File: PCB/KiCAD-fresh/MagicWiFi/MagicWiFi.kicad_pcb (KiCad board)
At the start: 2 copper layers, 6 parts

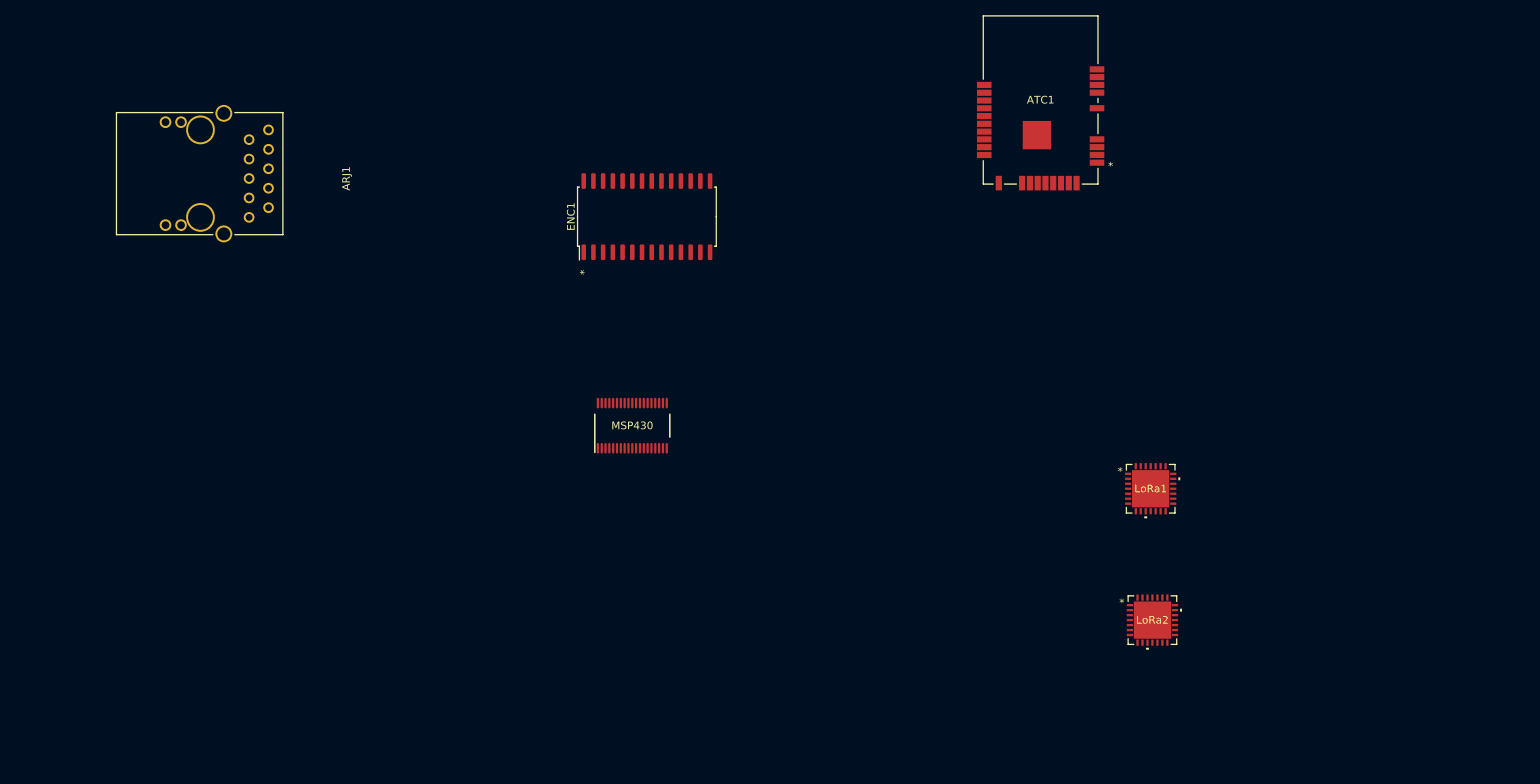
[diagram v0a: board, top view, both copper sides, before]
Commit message: Added basic layout
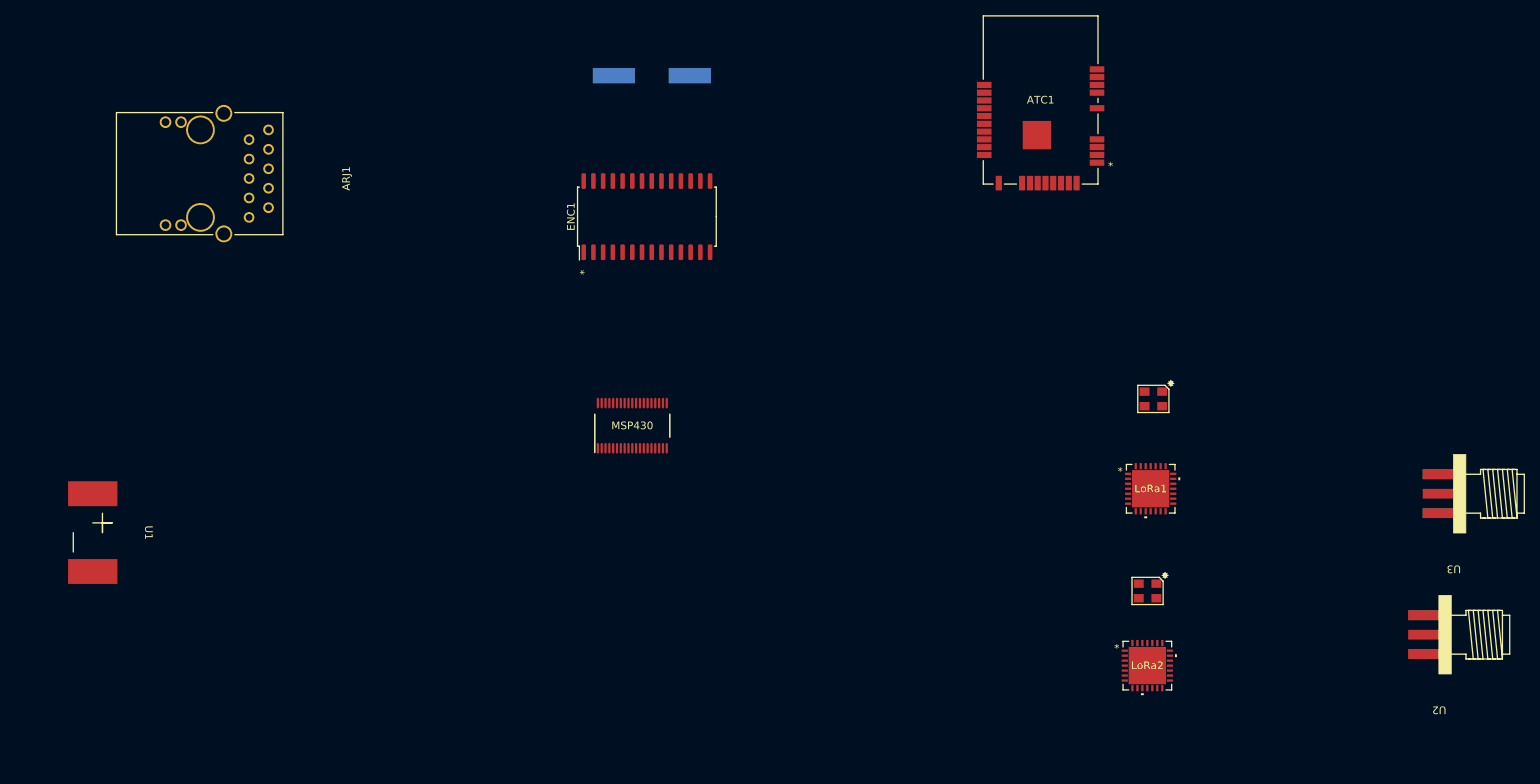
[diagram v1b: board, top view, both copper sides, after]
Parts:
- added U1: ~, MagicWiFi:Barrel_Conn, F.Cu at (38.1, 99.1)
- added U2: ~, MagicWiFi:SMA_EDGELAUNCH, F.Cu at (217.2, 112.4)
- added U3: ~, MagicWiFi:SMA_EDGELAUNCH, F.Cu at (219.1, 94.0)
- added X1: Osc, MagicWiFi:TCXO, F.Cu at (179.1, 106.7)
- added X2: Osc, MagicWiFi:TCXO, F.Cu at (179.8, 81.6)
- added X3: Osc, MagicWiFi:Xosc, B.Cu at (114.3, 39.4)
- moved LoRa2 5.98 mm to (179.0, 116.4)
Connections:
- ARJ1 pad 15: unconnected-(ARJ1-GND-Pad15) -> /GND
- ARJ1 pad 16: unconnected-(ARJ1-GND-Pad16) -> /GND
- ARJ1 pad 2: unconnected-(ARJ1-VC1--Pad2) -> /GND
- ARJ1 pad 7: unconnected-(ARJ1-VC1+-Pad7) -> /GND
- ATC1 pad 12: unconnected-(ATC1-GND_2-Pad12) -> /GND
- ATC1 pad 20: unconnected-(ATC1-VBAT-Pad20) -> /3v3
- ATC1 pad 23: unconnected-(ATC1-VDDIO-Pad23) -> /3v3
- ATC1 pad 28: unconnected-(ATC1-GND_3-Pad28) -> /GND
- ATC1 pad 29: unconnected-(ATC1-GND_PADDLE-Pad29) -> /GND
- ATC1 pad 9: unconnected-(ATC1-GND_1-Pad9) -> /GND
- ENC1 pad 11: unconnected-(ENC1-VSSRX-Pad11) -> /GND
- ENC1 pad 15: unconnected-(ENC1-VDDTX-Pad15) -> /3v3
- ENC1 pad 18: unconnected-(ENC1-VSSTX-Pad18) -> /GND
- ENC1 pad 19: unconnected-(ENC1-VDDRX-Pad19) -> /3v3
- ENC1 pad 2: unconnected-(ENC1-VSS-Pad2) -> /GND
- ENC1 pad 20: unconnected-(ENC1-VDDPLL-Pad20) -> /3v3
- ENC1 pad 21: unconnected-(ENC1-VSSPLL-Pad21) -> /GND
- ENC1 pad 22: unconnected-(ENC1-VSSOSC-Pad22) -> /GND
- ENC1 pad 25: unconnected-(ENC1-VDDOSC-Pad25) -> /3v3
- ENC1 pad 28: unconnected-(ENC1-VDD-Pad28) -> /3v3
- LoRa1 pad 1: unconnected-(LoRa1-VBAT1-Pad1) -> /3v3
- LoRa1 pad 15: unconnected-(LoRa1-VBAT2-Pad15) -> /3v3
- LoRa1 pad 16: unconnected-(LoRa1-GND-Pad16) -> /GND
- LoRa1 pad 22: unconnected-(LoRa1-GND-Pad22) -> /GND
- LoRa1 pad 26: unconnected-(LoRa1-GND-Pad26) -> /GND
- LoRa1 pad 29: unconnected-(LoRa1-GND-Pad29) -> /GND
- LoRa2 pad 1: unconnected-(LoRa2-VBAT1-Pad1) -> /3v3
- LoRa2 pad 15: unconnected-(LoRa2-VBAT2-Pad15) -> /3v3
- LoRa2 pad 16: unconnected-(LoRa2-GND-Pad16) -> /GND
- LoRa2 pad 22: unconnected-(LoRa2-GND-Pad22) -> /GND
- LoRa2 pad 26: unconnected-(LoRa2-GND-Pad26) -> /GND
- LoRa2 pad 29: unconnected-(LoRa2-GND-Pad29) -> /GND
- MSP430 pad 10: unconnected-(MSP430-DVCC-Pad10) -> /3v3
- MSP430 pad 11: unconnected-(MSP430-DVSS-Pad11) -> /GND

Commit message: part way through PCB design
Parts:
- added C1: 10uF, Resistor_SMD:R_0805_2012Metric_Pad1.20x1.40mm_HandSolder, F.Cu at (104.8, 66.7)
- added J1: 702461402, MagicWiFi:CON_702461402_MOL, F.Cu at (123.2, 120.0)
- added R1: 60, Resistor_SMD:R_0805_2012Metric_Pad1.20x1.40mm_HandSolder, F.Cu at (52.7, 39.4)
- added R2: 60, Resistor_SMD:R_0805_2012Metric_Pad1.20x1.40mm_HandSolder, F.Cu at (52.7, 65.4)
- added R3: 2.32k 1%, Resistor_SMD:R_0805_2012Metric_Pad1.20x1.40mm_HandSolder, F.Cu at (122.6, 67.3)
- added R4: 47k, Resistor_SMD:R_0805_2012Metric_Pad1.20x1.40mm_HandSolder, F.Cu at (43.8, 108.6)
- added SW1: SW_Push_Open, MagicWiFi:KSR223GNCLFG, F.Cu at (35.6, 114.3)
- moved BATT1 25.1 mm to (31.2, 123.2)
- renumbered U2 to AN1, U3 to AN2, U1 to BATT1
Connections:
- ARJ1 pad 11: unconnected-(ARJ1-LEDG+-Pad11) -> Net-(ARJ1-LEDG+)
- ARJ1 pad 12: unconnected-(ARJ1-LEDG--Pad12) -> /~LEDG
- ARJ1 pad 13: unconnected-(ARJ1-LEDY+-Pad13) -> Net-(ARJ1-LEDY+)
- ARJ1 pad 14: unconnected-(ARJ1-LEDY--Pad14) -> /~LEDY
- ENC1 pad 1: unconnected-(ENC1-VCAP-Pad1) -> Net-(ENC1-VCAP)
- ENC1 pad 14: unconnected-(ENC1-RBIAS-Pad14) -> Net-(ENC1-RBIAS)
- ENC1 pad 26: unconnected-(ENC1-LEDB-Pad26) -> /~LEDY
- ENC1 pad 27: unconnected-(ENC1-LEDA-Pad27) -> /~LEDG
- MSP430 pad 9: unconnected-(MSP430-RST_NMI_SBWTDIO_N-Pad9) -> Net-(MSP430-RST_NMI_SBWTDIO_N)

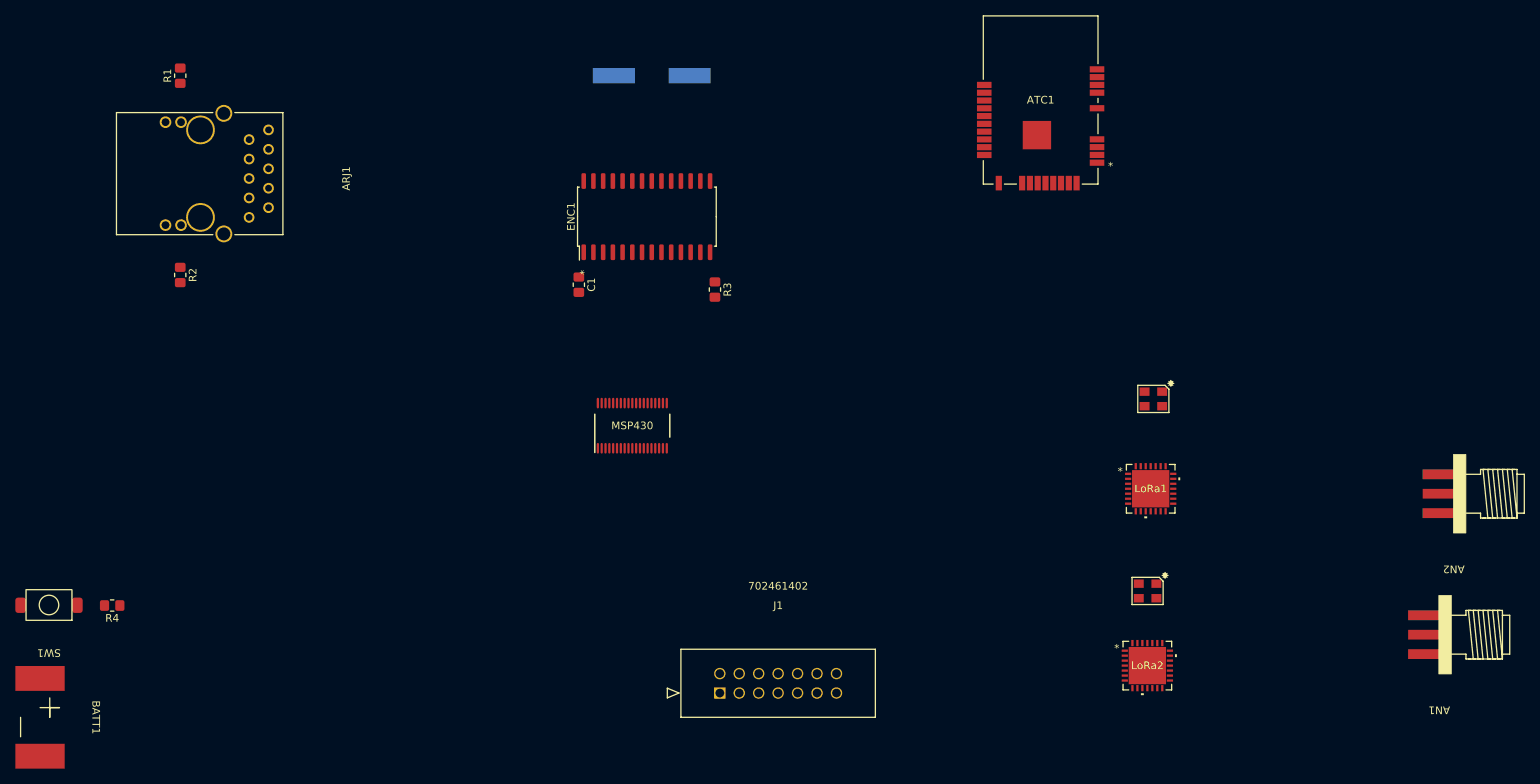
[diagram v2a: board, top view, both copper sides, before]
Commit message: Antenna Design Remade, stolen shamelessly from Sample design by SemTech (Mfgr), other traces routed and Documentation refreshed for components
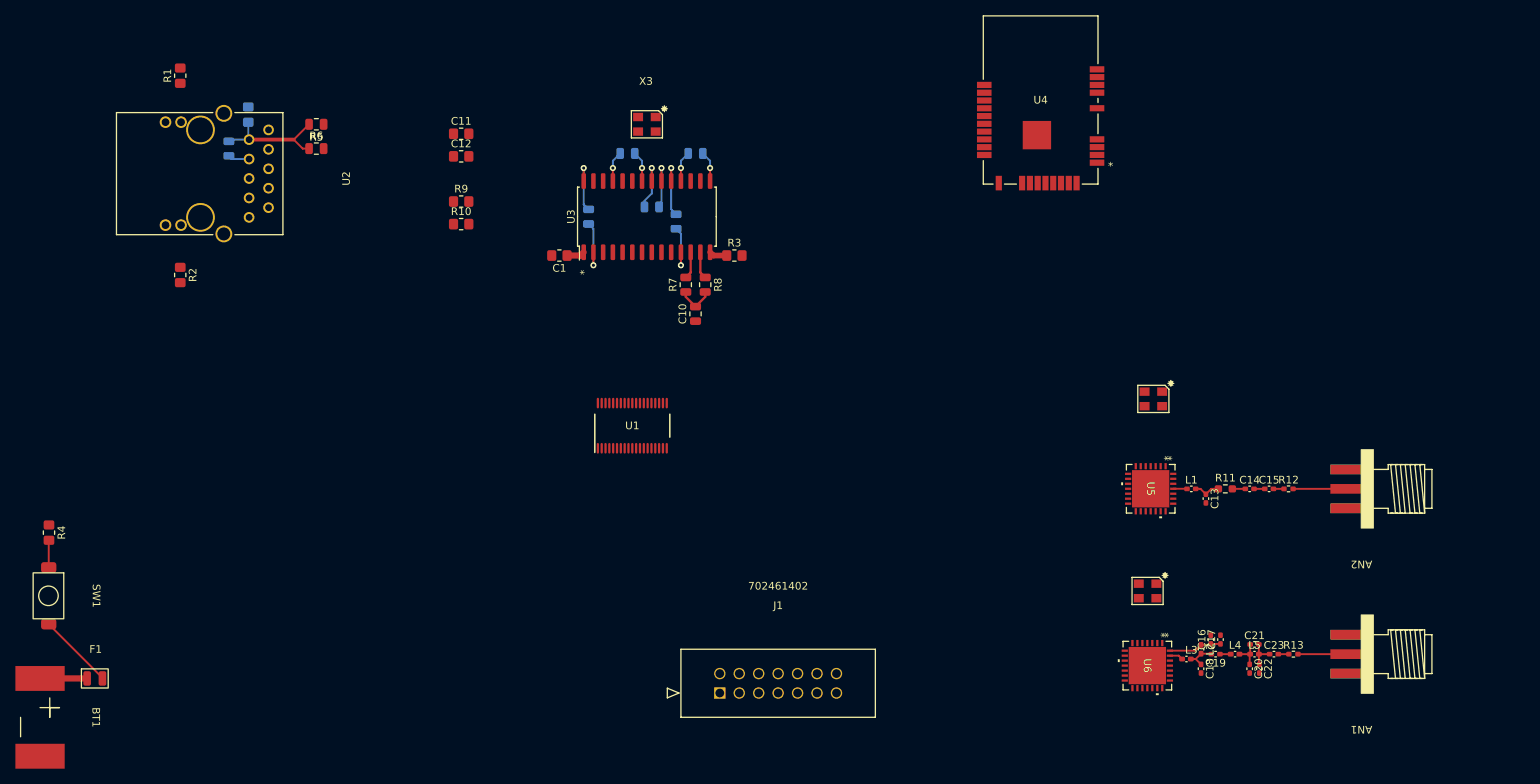
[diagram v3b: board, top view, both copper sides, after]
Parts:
- added C10: 0.1 uF, Capacitor_SMD:C_0805_2012Metric, F.Cu at (120.0, 70.5)
- added C11: 0.1 nF, Resistor_SMD:R_0805_2012Metric_Pad1.20x1.40mm_HandSolder, F.Cu at (89.4, 47.0)
- added C12: 0.1 nF, Resistor_SMD:R_0805_2012Metric_Pad1.20x1.40mm_HandSolder, F.Cu at (89.4, 49.9)
- added C13: 3.3 pF, Capacitor_SMD:C_0402_1005Metric_Pad0.74x0.62mm_HandSolder, F.Cu at (186.7, 94.6)
- added C14: 47 pF, Capacitor_SMD:C_0402_1005Metric_Pad0.74x0.62mm_HandSolder, F.Cu at (192.4, 93.3)
- added C15: 47 pF, Capacitor_SMD:C_0402_1005Metric_Pad0.74x0.62mm_HandSolder, F.Cu at (194.9, 93.3)
- added C16: 10 nF, Capacitor_SMD:C_0402_1005Metric_Pad0.74x0.62mm_HandSolder, F.Cu at (187.3, 113.0)
- added C17: 47 pF, Capacitor_SMD:C_0402_1005Metric_Pad0.74x0.62mm_HandSolder, F.Cu at (188.6, 113.0)
- added C18: 8.2 pF, Capacitor_SMD:C_0402_1005Metric_Pad0.74x0.62mm_HandSolder, F.Cu at (186.1, 116.8)
- added C19: 22 pF, Capacitor_SMD:C_0402_1005Metric_Pad0.74x0.62mm_HandSolder, F.Cu at (188.0, 114.9)
- added C20: 8.2 pF, Capacitor_SMD:C_0402_1005Metric_Pad0.74x0.62mm_HandSolder, F.Cu at (192.4, 116.8)
- added C21: 1.5 pF, Capacitor_SMD:C_0402_1005Metric_Pad0.74x0.62mm_HandSolder, F.Cu at (193.0, 113.7)
- added C22: 3.3 pF, Capacitor_SMD:C_0402_1005Metric_Pad0.74x0.62mm_HandSolder, F.Cu at (193.7, 116.8)
- added C23: 47 pF, Capacitor_SMD:C_0402_1005Metric_Pad0.74x0.62mm_HandSolder, F.Cu at (195.6, 114.9)
- added C4: 0.1 uF, Capacitor_SMD:C_0805_2012Metric, B.Cu at (59.1, 48.9)
- added C5: 0.1 uF, Capacitor_SMD:C_0805_2012Metric, B.Cu at (117.5, 58.4)
- added C6: 0.1 uF, Capacitor_SMD:C_0805_2012Metric, B.Cu at (120.0, 49.5)
- added C7: 0.1 uF, Capacitor_SMD:C_0805_2012Metric, B.Cu at (111.1, 49.5)
- added C8: 0.1 uF, Capacitor_SMD:C_0805_2012Metric, B.Cu at (114.3, 56.5)
- added C9: 0.1 uF, Capacitor_SMD:C_0805_2012Metric, B.Cu at (106.0, 57.8)
- added F1: Polyfuse, MagicWiFi:Fuse_BelFuse_0ZCJ0_1206_Metric_3216, F.Cu at (41.5, 118.1)
- added FB1: 80 mA min, Resistor_SMD:R_0805_2012Metric_Pad1.20x1.40mm_HandSolder, B.Cu at (61.6, 44.5)
- added L1: 10 nH, Capacitor_SMD:C_0402_1005Metric_Pad0.74x0.62mm_HandSolder, F.Cu at (184.8, 93.3)
- added L2: 33 nH, Inductor_SMD:L_0402_1005Metric_Pad0.77x0.64mm_HandSolder, F.Cu at (186.1, 114.3)
- added L3: 2.7 nH, Inductor_SMD:L_0402_1005Metric_Pad0.77x0.64mm_HandSolder, F.Cu at (184.2, 115.6)
- added L4: 5.6 nH, Inductor_SMD:L_0402_1005Metric_Pad0.77x0.64mm_HandSolder, F.Cu at (190.5, 114.9)
- added L5: 5.6 nH, Inductor_SMD:L_0402_1005Metric_Pad0.77x0.64mm_HandSolder, F.Cu at (193.0, 114.9)
- added R10: 75 Ohm, Resistor_SMD:R_0805_2012Metric_Pad1.20x1.40mm_HandSolder, F.Cu at (89.4, 58.8)
- added R11: 0R, Resistor_SMD:R_0603_1608Metric_Pad0.98x0.95mm_HandSolder, F.Cu at (189.2, 93.3)
- added R12: 0R, Resistor_SMD:R_0402_1005Metric_Pad0.72x0.64mm_HandSolder, F.Cu at (197.5, 93.3)
- added R13: 0R, Resistor_SMD:R_0402_1005Metric_Pad0.72x0.64mm_HandSolder, F.Cu at (198.1, 114.9)
- added R5: 49.9 Ohm, Capacitor_SMD:C_0805_2012Metric, F.Cu at (70.5, 45.7)
- added R6: 49.9 Ohm, Capacitor_SMD:C_0805_2012Metric, F.Cu at (70.5, 48.9)
- added R7: 49.9 Ohm, Capacitor_SMD:C_0805_2012Metric, F.Cu at (118.7, 66.7)
- added R8: 49.9 Ohm, Capacitor_SMD:C_0805_2012Metric, F.Cu at (121.3, 66.7)
- added R9: 75 Ohm, Resistor_SMD:R_0805_2012Metric_Pad1.20x1.40mm_HandSolder, F.Cu at (89.4, 55.8)
- SW1: value SW_Push_Open -> SPST-NC
- U1: renamed from MSP430; value MSP430FR2355TDBTR -> MSP430
- U2: renamed from ARJ1; value ARJM11C7-114-BA-EW2 -> ARJ1
- U3: renamed from ENC1; value ENC28J60x-SO -> ENC
- U4: renamed from ATC1; value ATWINC1500-MR210PB1952-T -> ATC
- U5: renamed from LoRa1; value SX1272IMLTRT -> LoRa1
- U6: renamed from LoRa2; value SX1272IMLTRT -> LoRa2
- X3: footprint MagicWiFi:Xosc -> MagicWiFi:TCXO; moved to F.Cu
- moved R4 12.6 mm to (35.6, 99.1), turned to -90 degrees
- moved AN2 12.1 mm to (207.0, 93.3)
- moved AN1 10.5 mm to (207.0, 114.9)
- moved SW1 8.98 mm to (41.2, 107.3), turned to -90 degrees
- moved X3 6.38 mm to (113.7, 45.7), turned to 0 degrees
- moved R3 5.12 mm to (125.1, 62.9), turned to 0 degrees
- moved C1 4.58 mm to (102.2, 62.9), turned to 180 degrees
- turned U5 to -90 degrees
- turned U6 to -90 degrees
- renumbered BATT1 to BT1
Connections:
- net /~LEDG renamed /LEDGN
- net /~LEDY renamed /LEDYN
- AN1 pad 1: unconnected-(AN1-In-Pad1) -> Net-(AN1-In)
- AN1 pad 2: unconnected-(AN1-GND-Pad2) -> GND
- AN1 pad 3: unconnected-(AN1-GND-Pad3) -> GND
- AN1 pad 4: unconnected-(AN1-GND-Pad4) -> GND
- AN1 pad 5: unconnected-(AN1-GND-Pad5) -> GND
- AN2 pad 1: unconnected-(AN2-In-Pad1) -> Net-(AN2-In)
- AN2 pad 2: unconnected-(AN2-GND-Pad2) -> GND
- AN2 pad 3: unconnected-(AN2-GND-Pad3) -> GND
- AN2 pad 4: unconnected-(AN2-GND-Pad4) -> GND
- AN2 pad 5: unconnected-(AN2-GND-Pad5) -> GND
- BT1 pad 1: /3v3 -> Net-(BT1-Inner1)
- BT1 pad 2: /GND -> GND
- C1 pad 2: /GND -> GND
- J1 pad 1: unconnected-(J1-Pad1) -> /ETH_MOSI
- J1 pad 10: unconnected-(J1-Pad10) -> /~MSP_RST
- J1 pad 2: unconnected-(J1-Pad2) -> /MSP_VCC
- J1 pad 3: unconnected-(J1-Pad3) -> /ETH_MISO
- J1 pad 4: unconnected-(J1-Pad4) -> /MSP_VCC_TAR
- J1 pad 5: unconnected-(J1-Pad5) -> /ETH_CLK
- J1 pad 7: unconnected-(J1-Pad7) -> /~ETH_CHIPSEL
- J1 pad 8: unconnected-(J1-Pad8) -> /MSP_TEST
- J1 pad 9: unconnected-(J1-Pad9) -> GND
- R1 pad 2: /3v3 -> +3.3V
- R2 pad 2: /3v3 -> +3.3V
- R3 pad 2: /GND -> GND
- SW1 pad 2: /3v3 -> +3.3V
- U1 pad 10: /3v3 -> +3.3V
- U1 pad 11: /GND -> GND
- U2 pad 1: unconnected-(ARJ1-VC2--Pad1) -> /VC2ETH_N
- U2 pad 10: unconnected-(ARJ1-TD+-Pad10) -> /TD_P
- U2 pad 15: /GND -> GND
- U2 pad 16: /GND -> GND
- U2 pad 2: /GND -> GND
- U2 pad 3: unconnected-(ARJ1-RD--Pad3) -> /RD_N
- U2 pad 5: unconnected-(ARJ1-RD+-Pad5) -> /RD_P
- U2 pad 6: unconnected-(ARJ1-VC2+-Pad6) -> /VC2ETH_P
- U2 pad 7: /GND -> GND
- U2 pad 8: unconnected-(ARJ1-TD--Pad8) -> /TD_N
- U2 pad 9: unconnected-(ARJ1-TCT-Pad9) -> /TD_C
- U3 pad 10: unconnected-(ENC1-~{RESET}-Pad10) -> /~ETH_RST
- U3 pad 11: /GND -> GND
- U3 pad 12: unconnected-(ENC1-TPIN--Pad12) -> /RD_N
- U3 pad 13: unconnected-(ENC1-TPIN+-Pad13) -> /RD_P
- U3 pad 15: /3v3 -> +3.3V
- U3 pad 16: unconnected-(ENC1-TPOUT--Pad16) -> /TD_N
- U3 pad 17: unconnected-(ENC1-TPOUT+-Pad17) -> /TD_P
- U3 pad 18: /GND -> GND
- U3 pad 19: /3v3 -> +3.3V
- U3 pad 2: /GND -> GND
- U3 pad 20: /3v3 -> +3.3V
- U3 pad 21: /GND -> GND
- U3 pad 22: /GND -> GND
- U3 pad 23: unconnected-(ENC1-OSC1-Pad23) -> /OSC1_ETH
- U3 pad 25: /3v3 -> +3.3V
- U3 pad 28: /3v3 -> +3.3V
- U3 pad 4: unconnected-(ENC1-~{INT}-Pad4) -> /~ETH_IRQ
- U3 pad 6: unconnected-(ENC1-SO-Pad6) -> /ETH_MISO
- U3 pad 7: unconnected-(ENC1-SI-Pad7) -> /ETH_MOSI
- U3 pad 8: unconnected-(ENC1-SCK-Pad8) -> /ETH_CLK
- U3 pad 9: unconnected-(ENC1-~{CS}-Pad9) -> /~ETH_CHIPSEL
- U4 pad 12: /GND -> GND
- U4 pad 20: /3v3 -> +3.3V
- U4 pad 23: /3v3 -> +3.3V
- U4 pad 28: /GND -> GND
- U4 pad 29: /GND -> GND
- U4 pad 9: /GND -> GND
- U5 pad 1: /3v3 -> +3.3V
- U5 pad 15: /3v3 -> +3.3V
- U5 pad 16: /GND -> GND
- U5 pad 22: /GND -> GND
- U5 pad 25: unconnected-(LoRa1-RFI-Pad25) -> Net-(U5-RFI)
- U5 pad 26: /GND -> GND
- U5 pad 29: /GND -> GND
- U5 pad 4: unconnected-(LoRa1-XTA-Pad4) -> Net-(U5-XTA)
- U6 pad 1: /3v3 -> +3.3V
- U6 pad 15: /3v3 -> +3.3V
- U6 pad 16: /GND -> GND
- U6 pad 22: /GND -> GND
- U6 pad 26: /GND -> GND
- U6 pad 27: unconnected-(LoRa2-PA_BOOST-Pad27) -> Net-(U6-PA_BOOST)
- U6 pad 28: unconnected-(LoRa2-VR_PA-Pad28) -> Net-(U6-VR_PA)
- U6 pad 29: /GND -> GND
- U6 pad 4: unconnected-(LoRa2-XTA-Pad4) -> Net-(U6-XTA)
- X1 pad 2: (no net) -> GND
- X1 pad 3: unconnected-(X1-GND-Pad3) -> Net-(U6-XTA)
- X1 pad 4: unconnected-(X1-Vdc-Pad4) -> +3.3V
- X2 pad 2: (no net) -> GND
- X2 pad 3: unconnected-(X2-GND-Pad3) -> Net-(U5-XTA)
- X2 pad 4: unconnected-(X2-Vdc-Pad4) -> +3.3V
- X3 pad 2: unconnected-(X3-osc2-Pad2) -> GND
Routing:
- net +3.3V: track 0.00 -> 40.3 mm, vias 0 -> 5
- net GND: track 0.00 -> 32.1 mm, vias 0 -> 5
- net /TD_C: track 0.00 -> 16.2 mm
- net Net-(U6-VR_PA): track 0.00 -> 6.98 mm
- net Net-(AN1-In): track 0.00 -> 6.26 mm
- net Net-(BT1-Inner1): track 0.00 -> 6.16 mm
- net Net-(AN2-In): track 0.00 -> 4.99 mm
- net Net-(C10-Pad2): track 0.00 -> 4.87 mm
- net Net-(C18-Pad1): track 0.00 -> 4.61 mm
- net Net-(C21-Pad2): track 0.00 -> 4.04 mm
- net Net-(C20-Pad1): track 0.00 -> 4.03 mm
- net Net-(C13-Pad1): track 0.00 -> 3.61 mm
- net Net-(SW1-A): track 0.00 -> 3.57 mm
- net /RD_P: track 0.00 -> 3.55 mm
- net /RD_N: track 0.00 -> 3.55 mm
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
